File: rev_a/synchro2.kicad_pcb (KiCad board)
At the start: 2 copper layers, 98 parts, among them J1 UPDATE_ENABLE, SW1 RESET_BUTTON, U1 AS5050, U10 ELD207, U11 ELD207, U12 74XX74, U13 L298, U14 L298, U15 MCP48X2, U16 MCP6542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

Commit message: Almost done with Rev. A.
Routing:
- net /Motor_Power/MB_MGND: track 218.2 -> 249.7 mm
- net GND: track 159.6 -> 182.1 mm
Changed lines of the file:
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@@
 (kicad_pcb (version 3) (host pcbnew "(2014-02-21 BZR 4712)-product")
   (general
-    (links 290)
+    (links 292)
     (no_connects 0)
     (area 49.544671 50.149999 150.399044 151.3015)
     (thickness 1.6)
     (drawings 41)
-    (tracks 1404)
+    (tracks 1425)
     (zones 0)
     (modules 98)
@@
   )
   (setup
-    (last_trace_width 0.2032)
+    (last_trace_width 1.27)
     (user_trace_width 0.2032)
     (user_trace_width 0.508)
@@
     (tags "CMD DPACK")
     (attr smd)
-    (fp_text reference U3 (at -0.025 1.905 360) (layer F.SilkS)
+    (fp_text reference U3 (at 0.08 1.01 360) (layer F.SilkS)
       (effects (font (size 1.016 1.016) (thickness 0.2032)))
     )
@@
     (pad 2 smd rect (at 0 -6.64972 270) (size 6.7 6.7) (layers F.Cu)
       (net 46 GND))
+    (pad 2 smd rect (at 0 -6.64972 270) (size 6.7 6.7) (layers B.Cu)
+      (net 46 GND))
     (model smd/dpack_2.wrl
       (at (xyz 0 0 0))
@@
     (tags "CMD DPACK")
     (attr smd)
-    (fp_text reference U7 (at 0.08 -11.59 360) (layer F.SilkS)
+    (fp_text reference U7 (at 0.08 1.01 360) (layer F.SilkS)
       (effects (font (size 1.016 1.016) (thickness 0.2032)))
     )
@@
     (pad 2 smd rect (at 0 -6.64972 270) (size 6.7 6.7) (layers F.Cu)
       (net 18 /Motor_Power/MB_MGND))
+    (pad 2 smd rect (at 0 -6.64972 270) (size 6.7 6.7) (layers B.Cu)
+      (net 18 /Motor_Power/MB_MGND))
     (model smd/dpack_2.wrl
       (at (xyz 0 0 0))
@@
   (segment (start 120.38476 133.2371) (end 121.9629 133.2371) (width 0.2032) (layer F.Cu) (net 17))
   (segment (start 130.425 122.295) (end 130.425 114.4143) (width 0.2032) (layer F.Cu) (net 17))
+  (segment (start 92.87472 64.085) (end 96.585 64.085) (width 1.27) (layer B.Cu) (net 18))
+  (segment (start 96.725 64.255) (end 96.565 64.095) (width 1.27) (layer B.Cu) (net 18))
+  (segment (start 96.725 67.505) (end 96.725 64.255) (width 1.27) (layer B.Cu) (net 18))
+  (segment (start 96.445 67.785) (end 96.725 67.505) (width 1.27) (layer B.Cu) (net 18))
+  (segment (start 90.785 67.785) (end 96.445 67.785) (width 1.27) (layer B.Cu) (net 18))
+  (segment (start 89.205 66.205) (end 90.785 67.785) (width 1.27) (layer B.Cu) (net 18))
+  (segment (start 89.205 60.625) (end 89.205 66.205) (width 1.27) (layer B.Cu) (net 18))
+  (segment (start 89.465 60.365) (end 89.205 60.625) (width 1.27) (layer B.Cu) (net 18))
+  (segment (start 95.035 60.365) (end 89.465 60.365) (width 1.27) (layer B.Cu) (net 18))
+  (segment (start 96.715 62.045) (end 95.035 60.365) (width 1.27) (layer B.Cu) (net 18))
+  (segment (start 96.715 63.955) (end 96.715 62.045) (width 1.27) (layer B.Cu) (net 18))
+  (segment (start 96.585 64.085) (end 96.715 63.955) (width 1.27) (layer B.Cu) (net 18))
   (segment (start 80.775 66.7629) (end 79.2629 66.7629) (width 1.27) (layer F.Cu) (net 18))
   (segment (start 77.28022 63.75022) (end 75.74 63.75022) (width 1.27) (layer F.Cu) (net 18))
@@
   (segment (start 112.5235 74.5265) (end 112.5235 73.83996) (width 0.508) (layer F.Cu) (net 45))
   (segment (start 111.725 75.325) (end 112.5235 74.5265) (width 0.508) (layer F.Cu) (net 45))
+  (segment (start 118.073053 66.383333) (end 118.073053 67.886947) (width 1.27) (layer B.Cu) (net 46))
+  (segment (start 118.073053 60.936947) (end 118.073053 61.91667) (width 1.27) (layer B.Cu) (net 46))
+  (segment (start 118.585 60.425) (end 118.073053 60.936947) (width 1.27) (layer B.Cu) (net 46))
+  (segment (start 112.555 60.425) (end 118.585 60.425) (width 1.27) (layer B.Cu) (net 46))
+  (segment (start 112.115 60.865) (end 112.555 60.425) (width 1.27) (layer B.Cu) (net 46))
+  (segment (start 112.115 67.635) (end 112.115 60.865) (width 1.27) (layer B.Cu) (net 46))
+  (segment (start 112.345 67.865) (end 112.115 67.635) (width 1.27) (layer B.Cu) (net 46))
+  (segment (start 118.051106 67.865) (end 112.345 67.865) (width 1.27) (layer B.Cu) (net 46))
+  (segment (start 118.073053 67.886947) (end 118.051106 67.865) (width 1.27) (layer B.Cu) (net 46))
   (segment (start 84.7557 110.605) (end 83.51748 110.605) (width 0.508) (layer F.Cu) (net 46))
   (segment (start 83.51748 110.605) (end 83.35 110.77248) (width 0.508) (layer F.Cu) (net 46))
@@
   (segment (start 72.29894 52.64) (end 81.56 52.64) (width 0.2032) (layer F.Cu) (net 46))
   (segment (start 106.715 57.905) (end 105.08 56.27) (width 1.27) (layer B.Cu) (net 46))
-  (segment (start 105.835 61.155) (end 99.875 61.155) (width 0.2032) (layer B.Cu) (net 46))
-  (segment (start 99.875 61.155) (end 96.205 57.485) (width 0.2032) (layer B.Cu) (net 46))
+  (segment (start 106.125 60.865) (end 99.585 60.865) (width 0.2032) (layer B.Cu) (net 46))
+  (segment (start 99.585 60.865) (end 96.205 57.485) (width 0.2032) (layer B.Cu) (net 46))
   (segment (start 96.205 57.485) (end 96.205 55.745) (width 0.2032) (layer B.Cu) (net 46))
-  (segment (start 106.715 60.275) (end 105.835 61.155) (width 0.2032) (layer B.Cu) (net 46))
+  (segment (start 106.715 60.275) (end 106.125 60.865) (width 0.2032) (layer B.Cu) (net 46))
   (segment (start 102.84 66.6879) (end 101.1021 66.6879) (width 1.27) (layer F.Cu) (net 46))
   (via (at 101.095 66.695) (size 0.889) (layers F.Cu B.Cu) (net 46))

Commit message: Rev. A is ready.
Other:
- board outline added: 100 x 100 mm
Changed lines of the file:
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@@
     (links 292)
     (no_connects 0)
-    (area 49.544671 50.149999 150.399044 151.3015)
+    (area 49.544671 49.949999 150.399044 151.3015)
     (thickness 1.6)
-    (drawings 41)
+    (drawings 45)
     (tracks 1425)
     (zones 0)
@@
   )
   (setup
-    (last_trace_width 1.27)
+    (last_trace_width 0.2032)
     (user_trace_width 0.2032)
     (user_trace_width 0.508)
@@
     (visible_elements 7FFEFFFF)
     (pcbplotparams
-      (layerselection 16285697)
+      (layerselection 284721153)
       (usegerberextensions true)
       (excludeedgelayer true)
@@
     )
   )
+  (gr_line (start 50 50) (end 50 150) (angle 90) (layer Edge.Cuts) (width 0.1))
+  (gr_line (start 150 50) (end 50 50) (angle 90) (layer Edge.Cuts) (width 0.1))
+  (gr_line (start 150 150) (end 150 50) (angle 90) (layer Edge.Cuts) (width 0.1))
+  (gr_line (start 50 150) (end 150 150) (angle 90) (layer Edge.Cuts) (width 0.1))
   (gr_text "Synchro2 Motor Driver - Rev.  A\n(c) 2014 by Wayne C. Gramlich\nAll rights Reserved.  23Feb2014" (at 94.775 131.485) (layer B.SilkS)
     (effects (font (size 1.016 1.016) (thickness 0.2032)) (justify left mirror))

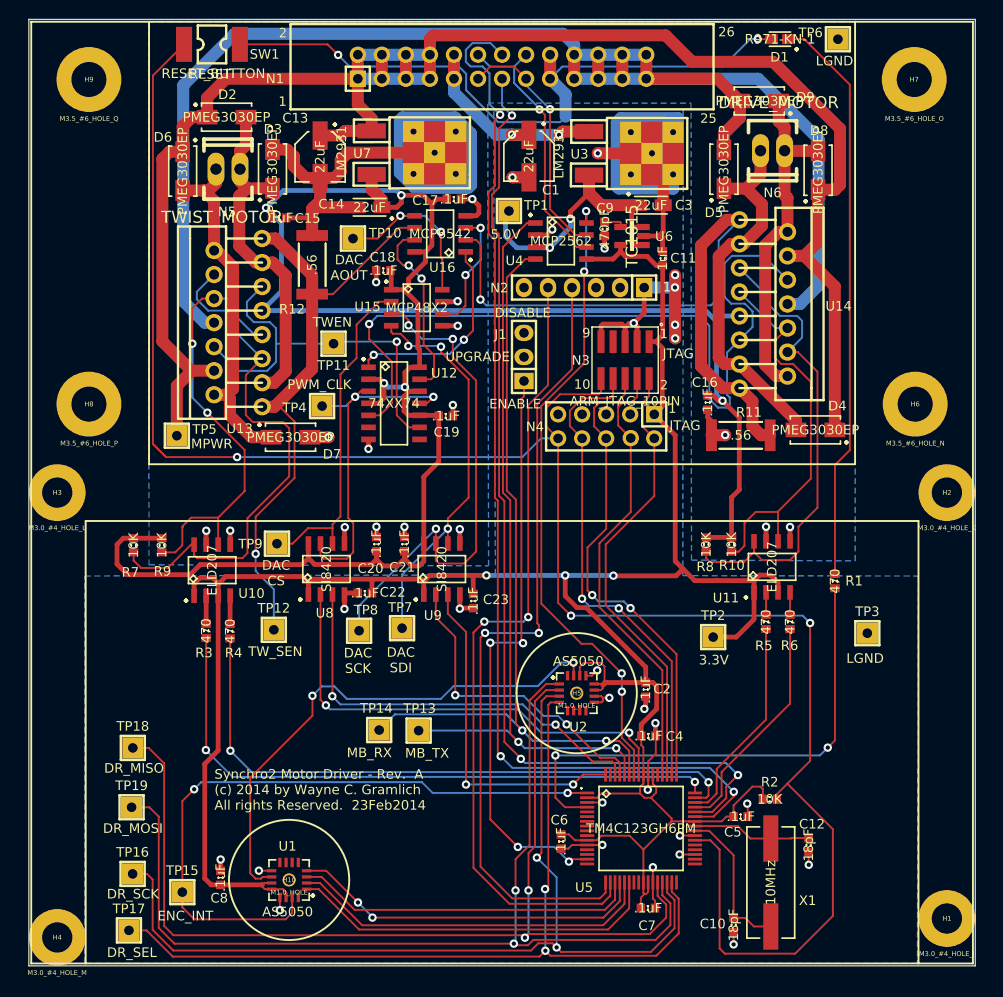
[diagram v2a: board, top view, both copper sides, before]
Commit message: Tweak compennt values to match pricing database.  No footprints were changed.
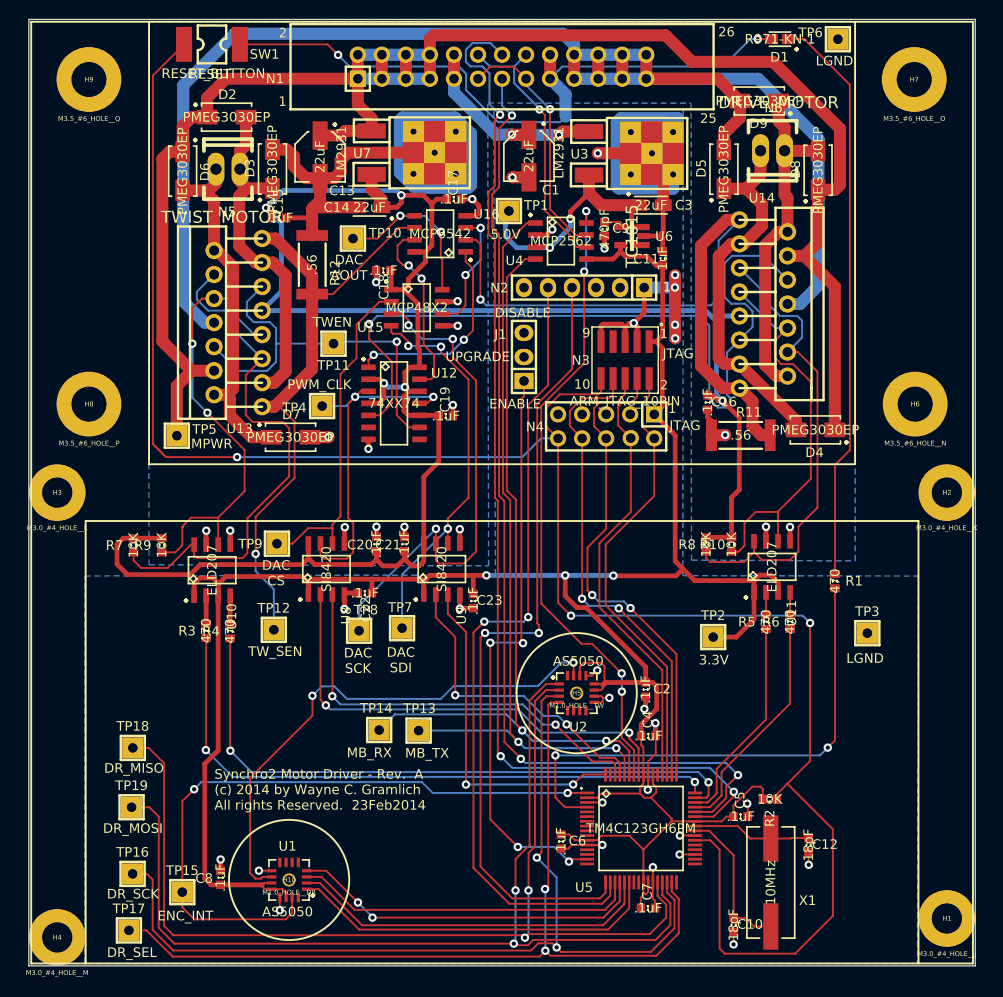
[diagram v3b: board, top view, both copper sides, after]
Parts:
- C1, C13: footprint IPC7351-Nominal:CAPAE530X540N -> Synchro2_Rev_A:CAPAE530X540N
- C10, C11, C12, C15, C16, C17, C18, C19, C2, C20, C21, C22, C23, C4, C5, C6, C7, C8, C9: footprint IPC7351-Nominal:CAPC1608X55N -> Synchro2_Rev_A:CAPC1608X55N
- C14, C3: footprint IPC7351-Nominal:CAPMP3216X180N -> Synchro2_Rev_A:CAPMP3216X180N
- D1: footprint IPC7351-Nominal:DIOM2012X160N -> Synchro2_Rev_A:DIOM2012X160N
- D2, D3, D4, D5, D6, D7, D8, D9: footprint IPC7351-Nominal:DIOM5027X244N -> Synchro2_Rev_A:DIOM5027X244N
- H1: value M3.0_#4_HOLE_J -> M3.0_#4_HOLE__J
- H10: value M1.0_HOLE -> M1.0_HOLE__DR
- H2: value M3.0_#4_HOLE_K -> M3.0_#4_HOLE__K
- H3: value M3.0_#4_HOLE_L -> M3.0_#4_HOLE__L
- H4: value M3.0_#4_HOLE_M -> M3.0_#4_HOLE__M
- H5: value M1.0_HOLE -> M1.0_HOLE__TW
- H6: value M3.5_#6_HOLE_N -> M3.5_#6_HOLE__N
- H7: value M3.5_#6_HOLE_O -> M3.5_#6_HOLE__O
- H8: value M3.5_#6_HOLE_P -> M3.5_#6_HOLE__P
- H9: value M3.5_#6_HOLE_Q -> M3.5_#6_HOLE__Q
- J1: footprint Pin_Headers:Pin_Header_Straight_1x03 -> Synchro2_Rev_A:Pin_Header_Straight_1x03
- N2: footprint Pin_Headers:Pin_Header_Straight_1x06 -> Synchro2_Rev_A:Pin_Header_Straight_1x06
- N5, N6: footprint Sockets_MOLEX_KK-System:Socket_MOLEX-KK-RM2-54mm_Lock_2pin_straight -> Synchro2_Rev_A:Socket_MOLEX-KK-RM2-54mm_Lock_2pin_straight
- R1, R10, R2, R3, R4, R5, R6, R7, R8, R9: footprint IPC7351-Nominal:RESC1608X50N -> Synchro2_Rev_A:RESC1608X50N
- R11, R12: footprint IPC7351-Nominal:RESC6432X76N -> Synchro2_Rev_A:RESC6432X76N
- SW1: footprint Robus:KSS221GLFS -> Synchro2_Rev_A:KSS221GLFS
- U10, U11, U15, U16, U4, U8, U9: footprint IPC7351-Nominal:SOIC127P600X175-8N -> Synchro2_Rev_A:SOIC127P600X175-8N
- U12: footprint IPC7351-Nominal:SOIC127P600X175-14N -> Synchro2_Rev_A:SOIC127P600X175-14N
- U13, U14: footprint Robus:MULTIWATT15 -> Synchro2_Rev_A:MULTIWATT15
- U5: footprint IPC7351-Nominal:QFP50P1200X1200X145-64N -> Synchro2_Rev_A:QFP50P1200X1200X145-64N
- U6: footprint Extra-Nominal:SOT95P280X145-5N -> Synchro2_Rev_A:SOT95P280X145-5N
- X1: footprint IPC7351-Nominal:XTAL1150X480X430N -> Synchro2_Rev_A:XTAL1150X480X430N
